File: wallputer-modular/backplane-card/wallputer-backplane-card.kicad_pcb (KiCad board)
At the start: 2 copper layers, 99.7 x 99.7 mm, 4 parts

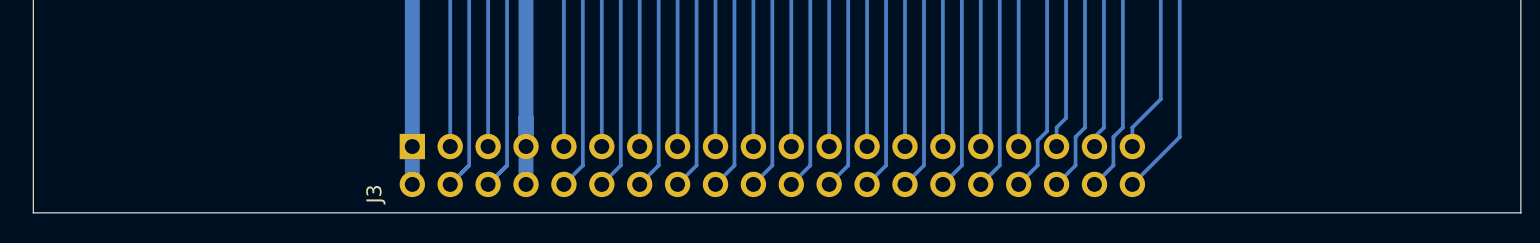
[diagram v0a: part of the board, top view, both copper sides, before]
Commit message: add card name
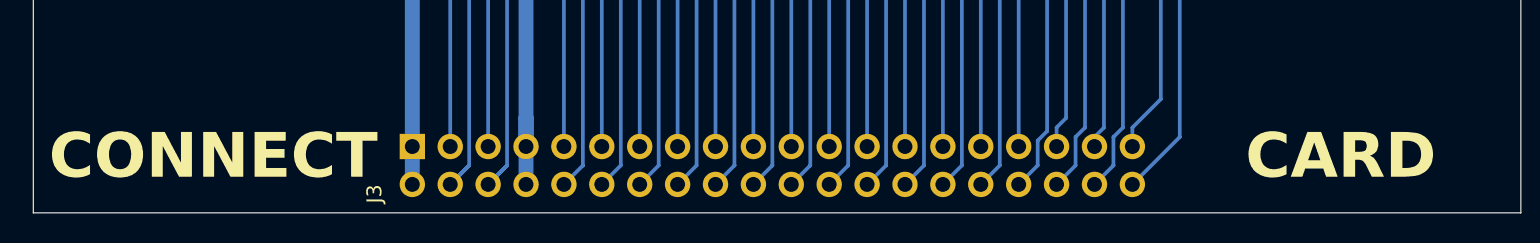
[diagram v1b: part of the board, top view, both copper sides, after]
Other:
- board text added: "CARD"
- board text added: "CONNECT"
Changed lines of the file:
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@@
 		(layer "Edge.Cuts")
+	)
+	(gr_text "CONNECT"
+		(at 50.8 146.685 0)
+		(layer "F.SilkS")
+		(effects
+			(font
+				(size 3 3)
+				(thickness 0.5)
+				(bold yes)
+			)
+		)
+	)
+	(gr_text "CARD\n"
+		(at 126.365 146.685 0)
+		(layer "F.SilkS")
+		(effects
+			(font
+				(size 3 3)
+				(thickness 0.5)
+				(bold yes)
+			)
+		)
 	)
 	(segment
